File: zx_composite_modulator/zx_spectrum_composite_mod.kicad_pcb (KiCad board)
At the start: 2 copper layers, 45 x 29 mm, 7 parts, among them J1 KLPX-0848A-2-B, Q1 BC547B

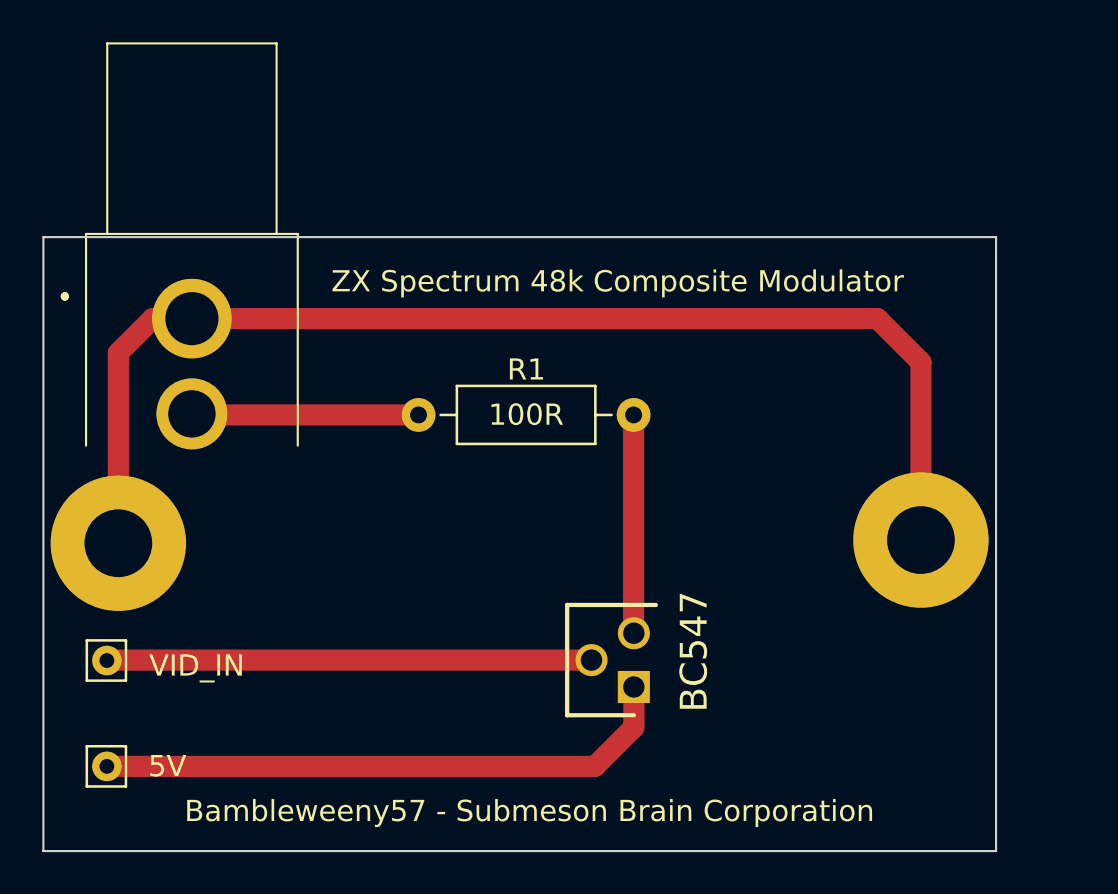
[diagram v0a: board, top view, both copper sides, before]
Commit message: reduced drill in coil
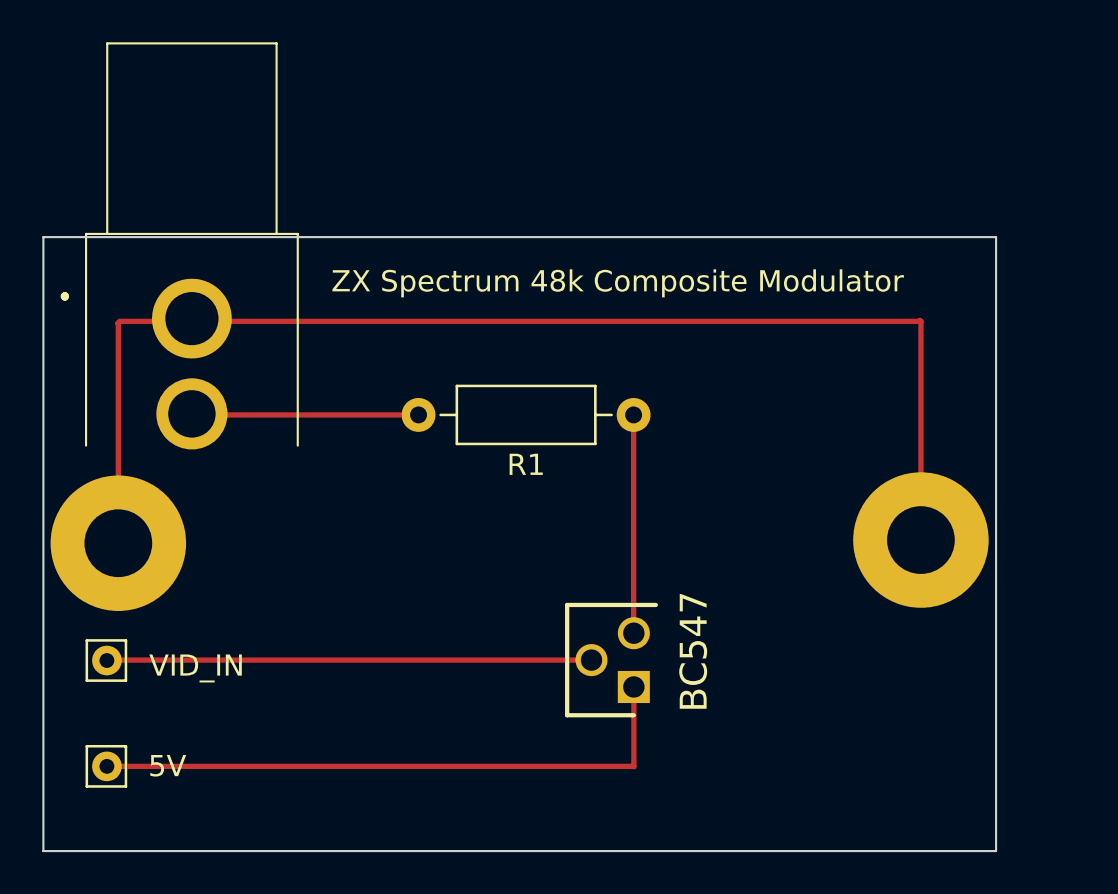
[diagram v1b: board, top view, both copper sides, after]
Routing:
- net GND: track 56.8 -> 58.7 mm
- net Net-(Q1-Pad1): track 27.6 -> 28.6 mm
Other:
- board text removed: "Bambleweeny57 - Submeson Brain Corporation"
